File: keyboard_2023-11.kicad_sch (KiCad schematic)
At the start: 76 parts, among them J1 Conn_01x04, J10 Conn_01x01_Socket, J11 Conn_01x07_Socket, J2 Conn_01x04_Socket, J3 Conn_01x07_Socket, J4 Conn_01x07_Pin, J5 Conn_01x01_Socket, J6 Conn_01x01_Socket, J7 Conn_01x01_Socket, J8 Conn_01x01_Socket, J9 Conn_01x01_Socket, SW1 SW_Push, SW10 SW_Push, SW11 SW_Push, SW12 SW_Push, SW13 SW_Push, SW14 SW_Push, SW15 SW_Push, SW16 SW_Push, SW17 SW_Push, SW18 SW_Push, SW19 SW_Push, SW2 SW_Push, SW20 SW_Push, SW21 SW_Push, SW22 SW_Push, SW23 SW_Push, SW24 SW_Push, SW3 SW_Push, SW4 SW_Push, SW5 SW_Push, SW6 SW_Push, SW7 SW_Push, SW8 SW_Push, SW9 SW_Push, U1 MCP23017_SO, U2 MCP23017_SO

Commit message: routed 90%
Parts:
- removed J10, J5, J6, J7, J8, J9: Conn_01x01_Socket, project-local:PinHeader_1x01_P2.54mm_Vertical, symbol Connector:Conn_01x01_Socket
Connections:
- net A0: now reaches JP4.2 (C), U2.15 (A0)
- net A0: now also JP1.2 (C), U1.15 (A0)
- net A1: now reaches JP2.2 (C), U1.16 (A1)
- net A1: now also JP5.2 (C), U2.16 (A1)
- net A2: now reaches JP3.2 (C), U1.17 (A2)
- net A2: now also JP6.2 (C), U2.17 (A2)
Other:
- moved on the sheet: J11, JP1, JP2, JP3, JP4, JP5, JP6, U1, U2

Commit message: snapshot
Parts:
- SW1, SW10, SW11, SW12, SW13, SW14, SW15, SW16, SW17, SW18, SW19, SW2, SW20, SW21, SW22, SW23, SW24, SW3, SW4, SW5, SW6, SW7, SW8, SW9: footprint keyswitches:SW_MX_reversible -> project-local:SW_MX_reversible
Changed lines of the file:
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@@
       (effects (font (size 1.27 1.27)))
     )
-    (property "Footprint" "keyswitches:SW_MX_reversible" (at 124.46 60.96 0)
+    (property "Footprint" "project-local:SW_MX_reversible" (at 124.46 60.96 0)
       (effects (font (size 1.27 1.27)) hide)
     )
@@
       (effects (font (size 1.27 1.27)))
     )
-    (property "Footprint" "keyswitches:SW_MX_reversible" (at 124.46 43.18 0)
+    (property "Footprint" "project-local:SW_MX_reversible" (at 124.46 43.18 0)
       (effects (font (size 1.27 1.27)) hide)
     )
@@
       (effects (font (size 1.27 1.27)))
     )
-    (property "Footprint" "keyswitches:SW_MX_reversible" (at 185.42 60.96 0)
+    (property "Footprint" "project-local:SW_MX_reversible" (at 185.42 60.96 0)
       (effects (font (size 1.27 1.27)) hide)
     )
@@
       (effects (font (size 1.27 1.27)))
     )
-    (property "Footprint" "keyswitches:SW_MX_reversible" (at 165.1 43.18 0)
+    (property "Footprint" "project-local:SW_MX_reversible" (at 165.1 43.18 0)
       (effects (font (size 1.27 1.27)) hide)
     )
@@
       (effects (font (size 1.27 1.27)))
     )
-    (property "Footprint" "keyswitches:SW_MX_reversible" (at 124.46 100.33 0)
+    (property "Footprint" "project-local:SW_MX_reversible" (at 124.46 100.33 0)
       (effects (font (size 1.27 1.27)) hide)
     )
@@
       (effects (font (size 1.27 1.27)))
     )
-    (property "Footprint" "keyswitches:SW_MX_reversible" (at 124.46 24.13 0)
+    (property "Footprint" "project-local:SW_MX_reversible" (at 124.46 24.13 0)
       (effects (font (size 1.27 1.27)) hide)
     )
@@
       (effects (font (size 1.27 1.27)))
     )
-    (property "Footprint" "keyswitches:SW_MX_reversible" (at 144.78 60.96 0)
+    (property "Footprint" "project-local:SW_MX_reversible" (at 144.78 60.96 0)
       (effects (font (size 1.27 1.27)) hide)
     )
@@
       (effects (font (size 1.27 1.27)))
     )
-    (property "Footprint" "keyswitches:SW_MX_reversible" (at 226.06 100.33 0)
+    (property "Footprint" "project-local:SW_MX_reversible" (at 226.06 100.33 0)
       (effects (font (size 1.27 1.27)) hide)
     )
@@
       (effects (font (size 1.27 1.27)))
     )
-    (property "Footprint" "keyswitches:SW_MX_reversible" (at 226.06 60.96 0)
+    (property "Footprint" "project-local:SW_MX_reversible" (at 226.06 60.96 0)
       (effects (font (size 1.27 1.27)) hide)
     )
@@
       (effects (font (size 1.27 1.27)))
     )
-    (property "Footprint" "keyswitches:SW_MX_reversible" (at 205.74 100.33 0)
+    (property "Footprint" "project-local:SW_MX_reversible" (at 205.74 100.33 0)
       (effects (font (size 1.27 1.27)) hide)
     )
@@
       (effects (font (size 1.27 1.27)))
     )
-    (property "Footprint" "keyswitches:SW_MX_reversible" (at 144.78 24.13 0)
+    (property "Footprint" "project-local:SW_MX_reversible" (at 144.78 24.13 0)
       (effects (font (size 1.27 1.27)) hide)
     )
@@
       (effects (font (size 1.27 1.27)))
     )
-    (property "Footprint" "keyswitches:SW_MX_reversible" (at 226.06 43.18 0)
+    (property "Footprint" "project-local:SW_MX_reversible" (at 226.06 43.18 0)
       (effects (font (size 1.27 1.27)) hide)
     )
@@
       (effects (font (size 1.27 1.27)))
     )
-    (property "Footprint" "keyswitches:SW_MX_reversible" (at 165.1 24.13 0)
+    (property "Footprint" "project-local:SW_MX_reversible" (at 165.1 24.13 0)
       (effects (font (size 1.27 1.27)) hide)
     )
@@
       (effects (font (size 1.27 1.27)))
     )
-    (property "Footprint" "keyswitches:SW_MX_reversible" (at 144.78 43.18 0)
+    (property "Footprint" "project-local:SW_MX_reversible" (at 144.78 43.18 0)
       (effects (font (size 1.27 1.27)) hide)
     )
@@
       (effects (font (size 1.27 1.27)))
     )
-    (property "Footprint" "keyswitches:SW_MX_reversible" (at 226.06 24.13 0)
+    (property "Footprint" "project-local:SW_MX_reversible" (at 226.06 24.13 0)
       (effects (font (size 1.27 1.27)) hide)
     )
@@
       (effects (font (size 1.27 1.27)))
     )
-    (property "Footprint" "keyswitches:SW_MX_reversible" (at 185.42 100.33 0)
+    (property "Footprint" "project-local:SW_MX_reversible" (at 185.42 100.33 0)
       (effects (font (size 1.27 1.27)) hide)
     )
@@
       (effects (font (size 1.27 1.27)))
     )
-    (property "Footprint" "keyswitches:SW_MX_reversible" (at 205.74 24.13 0)
+    (property "Footprint" "project-local:SW_MX_reversible" (at 205.74 24.13 0)
       (effects (font (size 1.27 1.27)) hide)
     )
@@
       (effects (font (size 1.27 1.27)))
     )
-    (property "Footprint" "keyswitches:SW_MX_reversible" (at 144.78 100.33 0)
+    (property "Footprint" "project-local:SW_MX_reversible" (at 144.78 100.33 0)
       (effects (font (size 1.27 1.27)) hide)
     )
@@
       (effects (font (size 1.27 1.27)))
     )
-    (property "Footprint" "keyswitches:SW_MX_reversible" (at 205.74 60.96 0)
+    (property "Footprint" "project-local:SW_MX_reversible" (at 205.74 60.96 0)
       (effects (font (size 1.27 1.27)) hide)
     )
@@
       (effects (font (size 1.27 1.27)))
     )
-    (property "Footprint" "keyswitches:SW_MX_reversible" (at 205.74 43.18 0)
+    (property "Footprint" "project-local:SW_MX_reversible" (at 205.74 43.18 0)
       (effects (font (size 1.27 1.27)) hide)
     )
@@
       (effects (font (size 1.27 1.27)))
     )
-    (property "Footprint" "keyswitches:SW_MX_reversible" (at 185.42 24.13 0)
+    (property "Footprint" "project-local:SW_MX_reversible" (at 185.42 24.13 0)
       (effects (font (size 1.27 1.27)) hide)
     )
@@
       (effects (font (size 1.27 1.27)))
     )
-    (property "Footprint" "keyswitches:SW_MX_reversible" (at 185.42 43.18 0)
+    (property "Footprint" "project-local:SW_MX_reversible" (at 185.42 43.18 0)
       (effects (font (size 1.27 1.27)) hide)
     )
@@
       (effects (font (size 1.27 1.27)))
     )
-    (property "Footprint" "keyswitches:SW_MX_reversible" (at 165.1 100.33 0)
+    (property "Footprint" "project-local:SW_MX_reversible" (at 165.1 100.33 0)
       (effects (font (size 1.27 1.27)) hide)
     )
@@
       (effects (font (size 1.27 1.27)))
     )
-    (property "Footprint" "keyswitches:SW_MX_reversible" (at 165.1 60.96 0)
-      (effects (font (size 1.27 1.27)) hide)
-    )
+    (property "Footprint" "project-local:SW_MX_reversible" (at 165.1 60.96 0)
+      (effects (font (size 1.27 1.27)) hide)
+    )

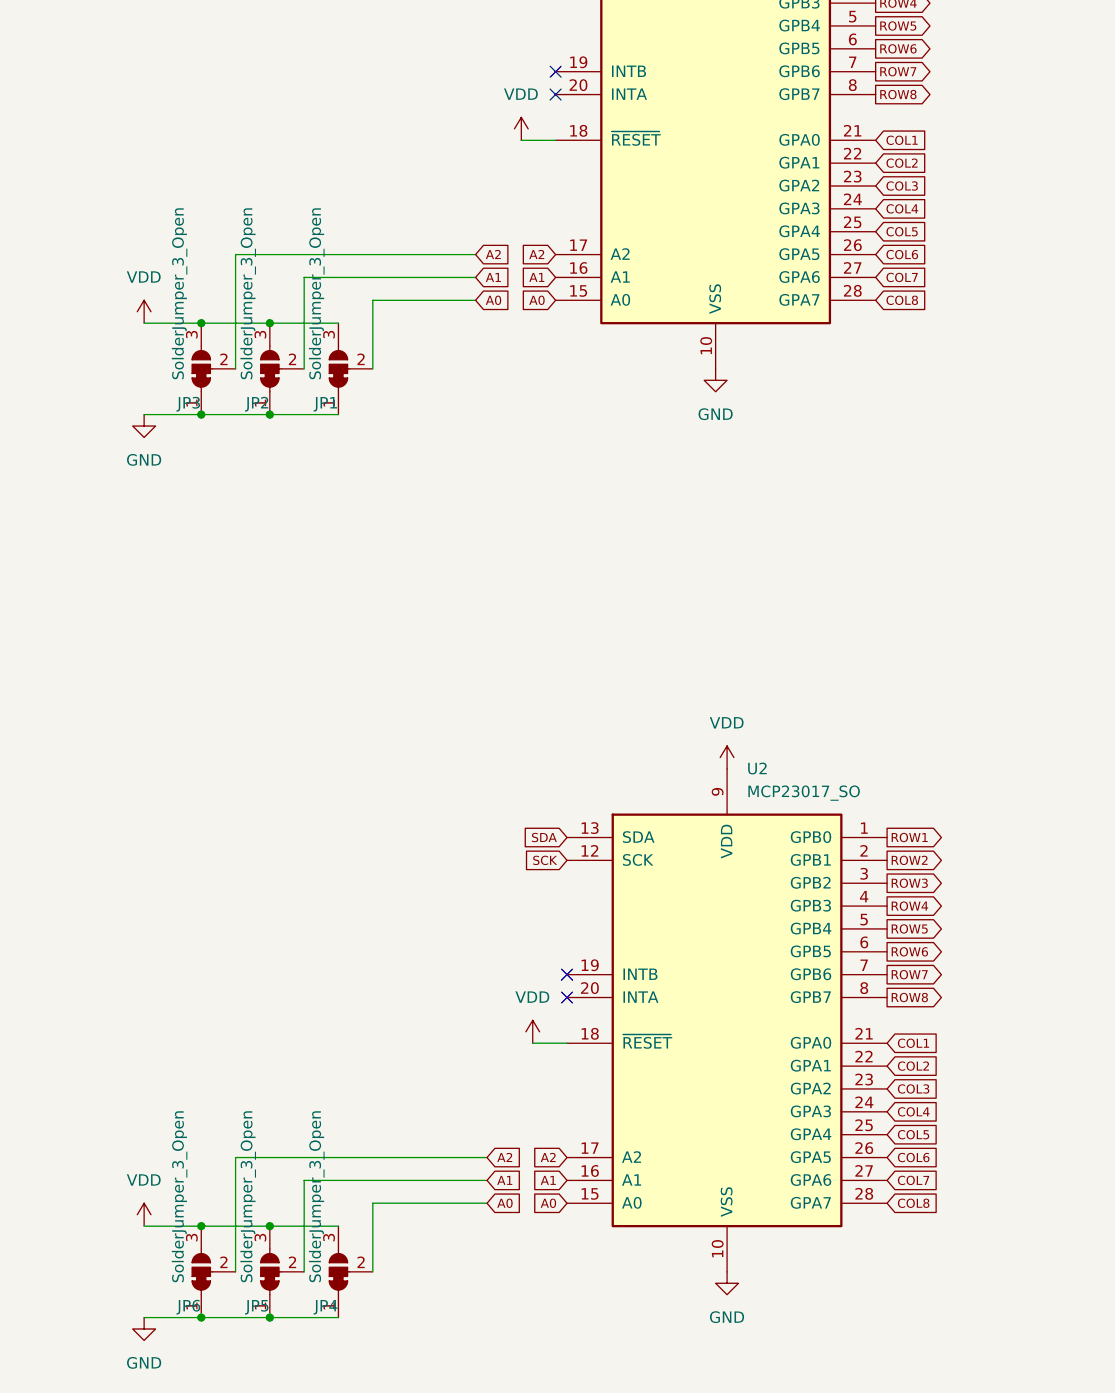
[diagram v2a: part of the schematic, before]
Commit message: fix solder jumpers
front/back io-expander need sepparate jumpers, as the already have preset values which might conflict with user selection = create a short.
switch solder jumpers to opposite side of board of the coresponding io-expander
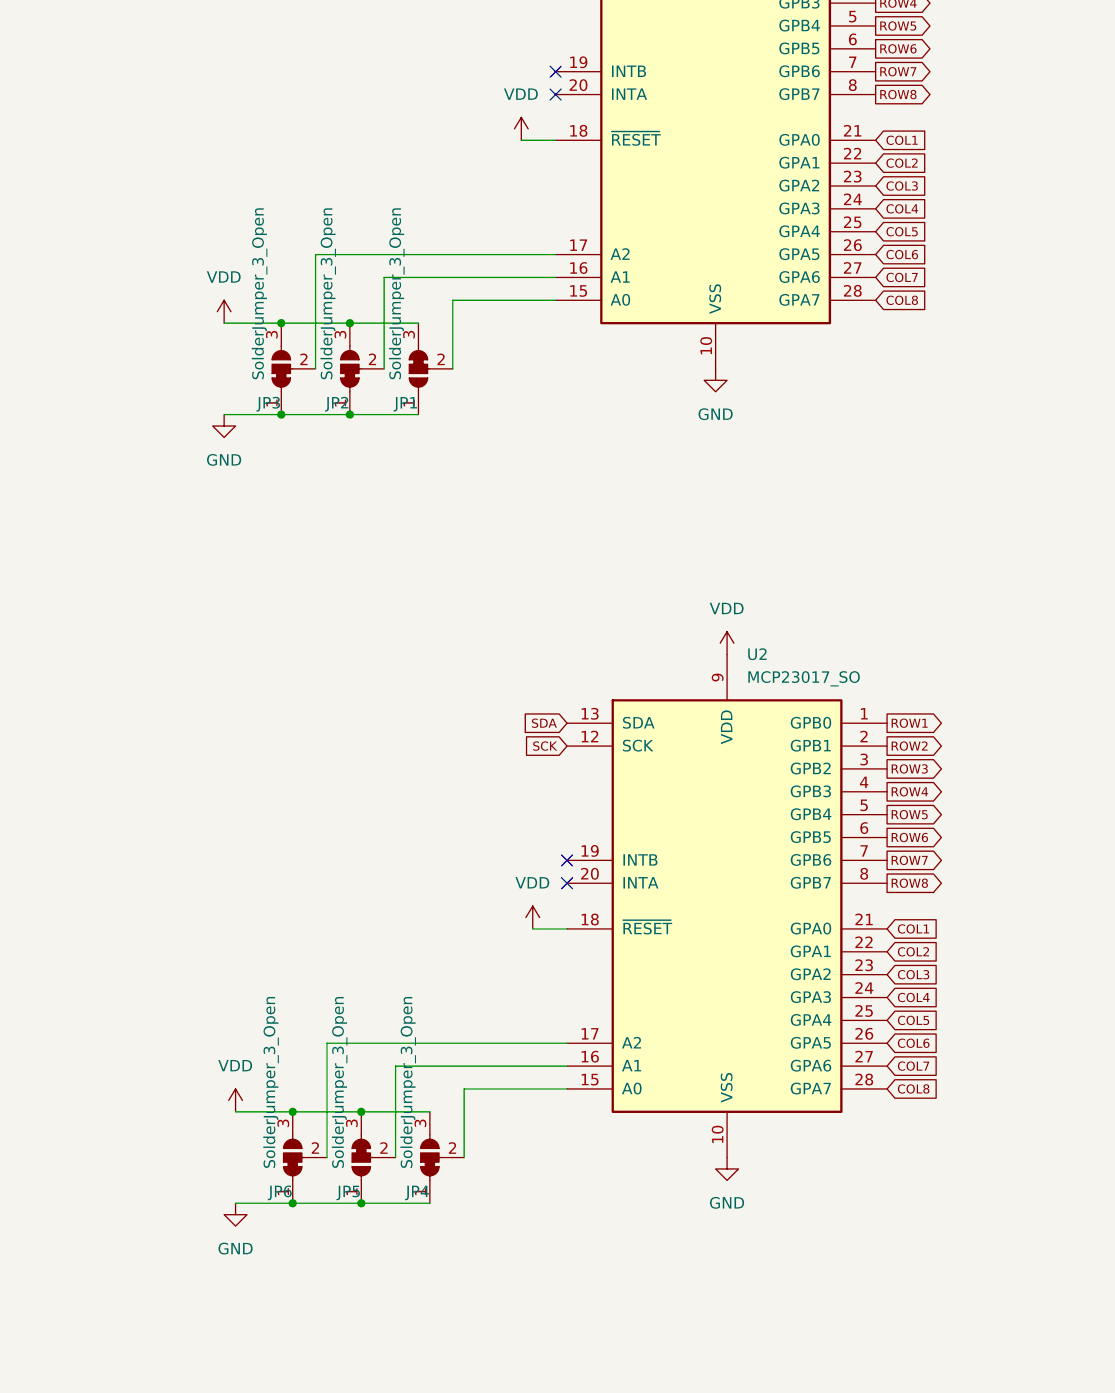
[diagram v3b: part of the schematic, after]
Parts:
- JP1, JP5: footprint Jumper:SolderJumper-3_P1.3mm_Bridged12_RoundedPad1.0x1.5mm_NumberLabels -> project-local:SolderJumper-3_P1.3mm_Bridged23_RoundedPad1.0x1.5mm_NumberLabels; symbol Jumper:SolderJumper_3_Bridged12 -> project-local:SolderJumper_3_Bridged23
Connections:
- net A0: no longer names the net of JP4.2 (C), U2.15 (A0)
- net A0: no longer JP1.2 (C), U1.15 (A0)
- net A1: no longer names the net of JP2.2 (C), U1.16 (A1)
- net A1: no longer JP5.2 (C), U2.16 (A1)
- net A2: no longer names the net of JP3.2 (C), U1.17 (A2)
- net A2: no longer JP6.2 (C), U2.17 (A2)
- new net: JP1.2 (C), U1.15 (A0)
- new net: JP5.2 (C), U2.16 (A1)
- new net: JP6.2 (C), U2.17 (A2)
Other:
- moved on the sheet: JP1, JP2, JP3, JP4, JP5, JP6, U2
